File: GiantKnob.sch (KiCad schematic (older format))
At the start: 65 parts

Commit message: First version of schematics
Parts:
- removed C? (x2): 1p, symbol device:C_Small
- removed R? (x2): 10k, symbol device:R_Small
- removed SW?: ENC1, symbol device:Rotary_Encoder_Switch
- removed SW?: ENC2, symbol device:Rotary_Encoder_Switch
- added SW4: ENC1, symbol device:Rotary_Encoder
- added SW7: ENC2, symbol device:Rotary_Encoder
- gave numbers to parts that had none: 53
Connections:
- net BTN1: now also U2.20 (PD2)
- net BTN2: now also U2.21 (PD3)
- net BTN3: now also U2.25 (PD4)
- net ENC1_A: now also U2.26 (PD6)
- net ENC1_B: now also U2.27 (PD7)
- net ENC2_A: now also U2.31 (PC6)
- net ENC2_B: now also U2.32 (PC7)
- net GND: now also SW4.C, SW7.C
- net VFO_A: now also U2.18 (PD0)
- net VFO_B: now also U2.19 (PD1)
- net VFO_BTN: now also U2.1 (PE6)
- net at C10.1, R8.2, U1.5: now also SW4.A
- net at C11.1, R9.2, U1.9: now also SW4.B
- net at C15.1, R14.2, U1.11: now also SW7.A
- net at C16.1, R15.2, U1.13: now also SW7.B
- no-connect marks 0 -> 10
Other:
- moved on the sheet: D4, R13, R17

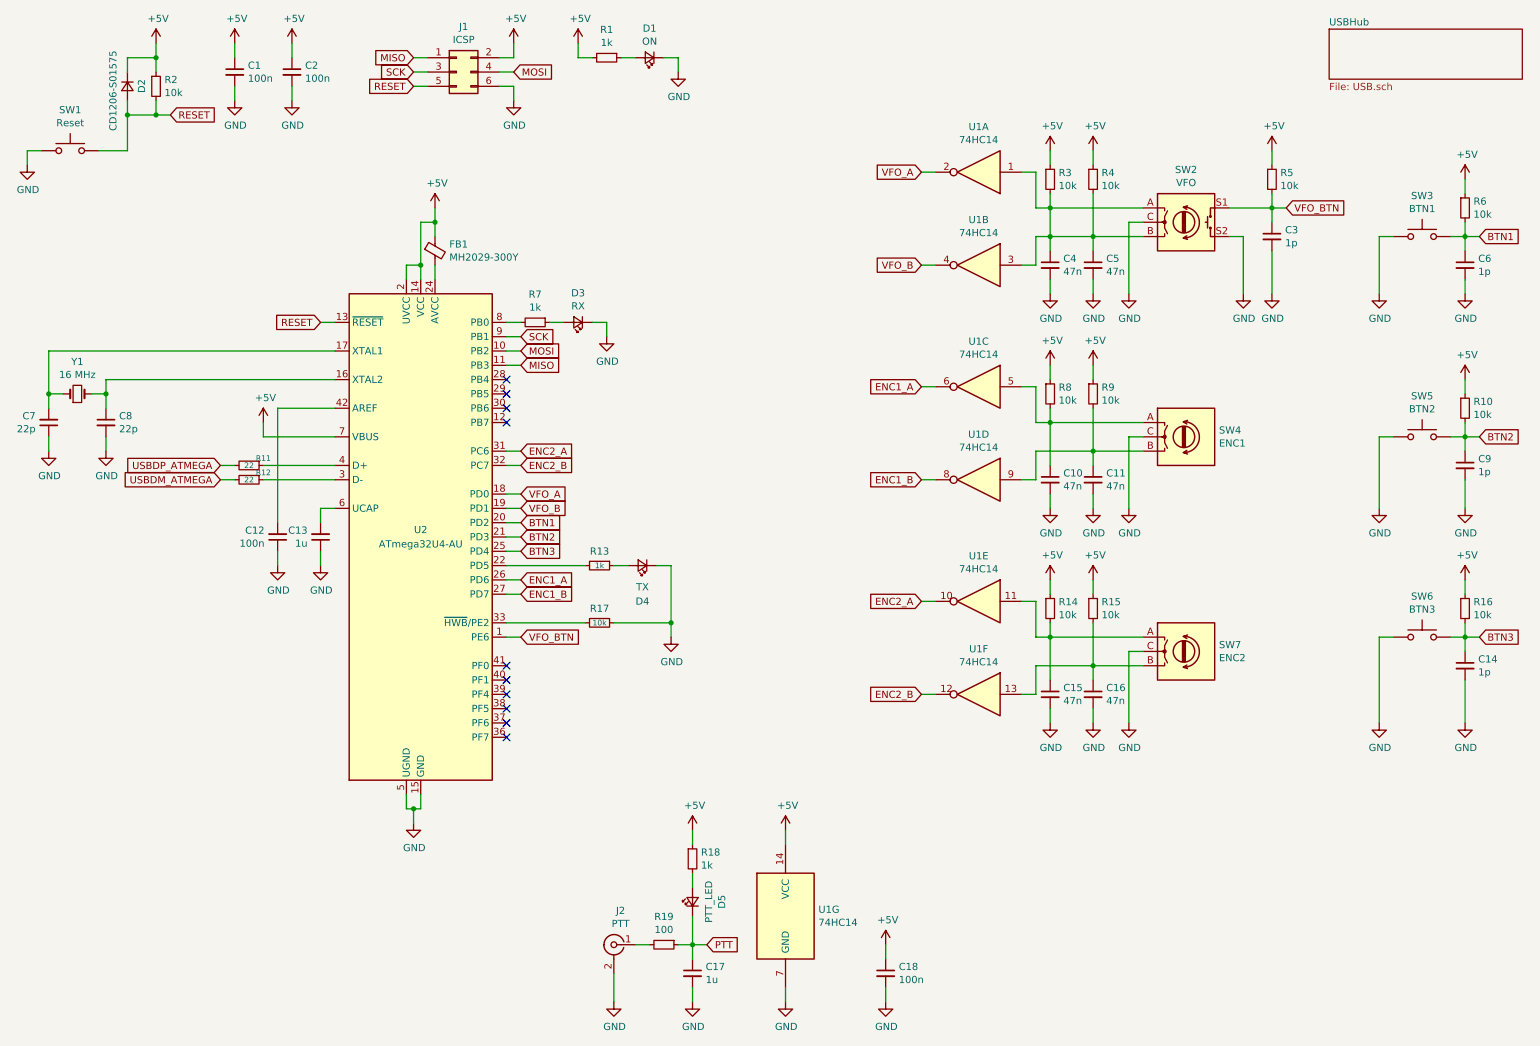
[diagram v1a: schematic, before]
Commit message: Added PTT to ATmega32U4
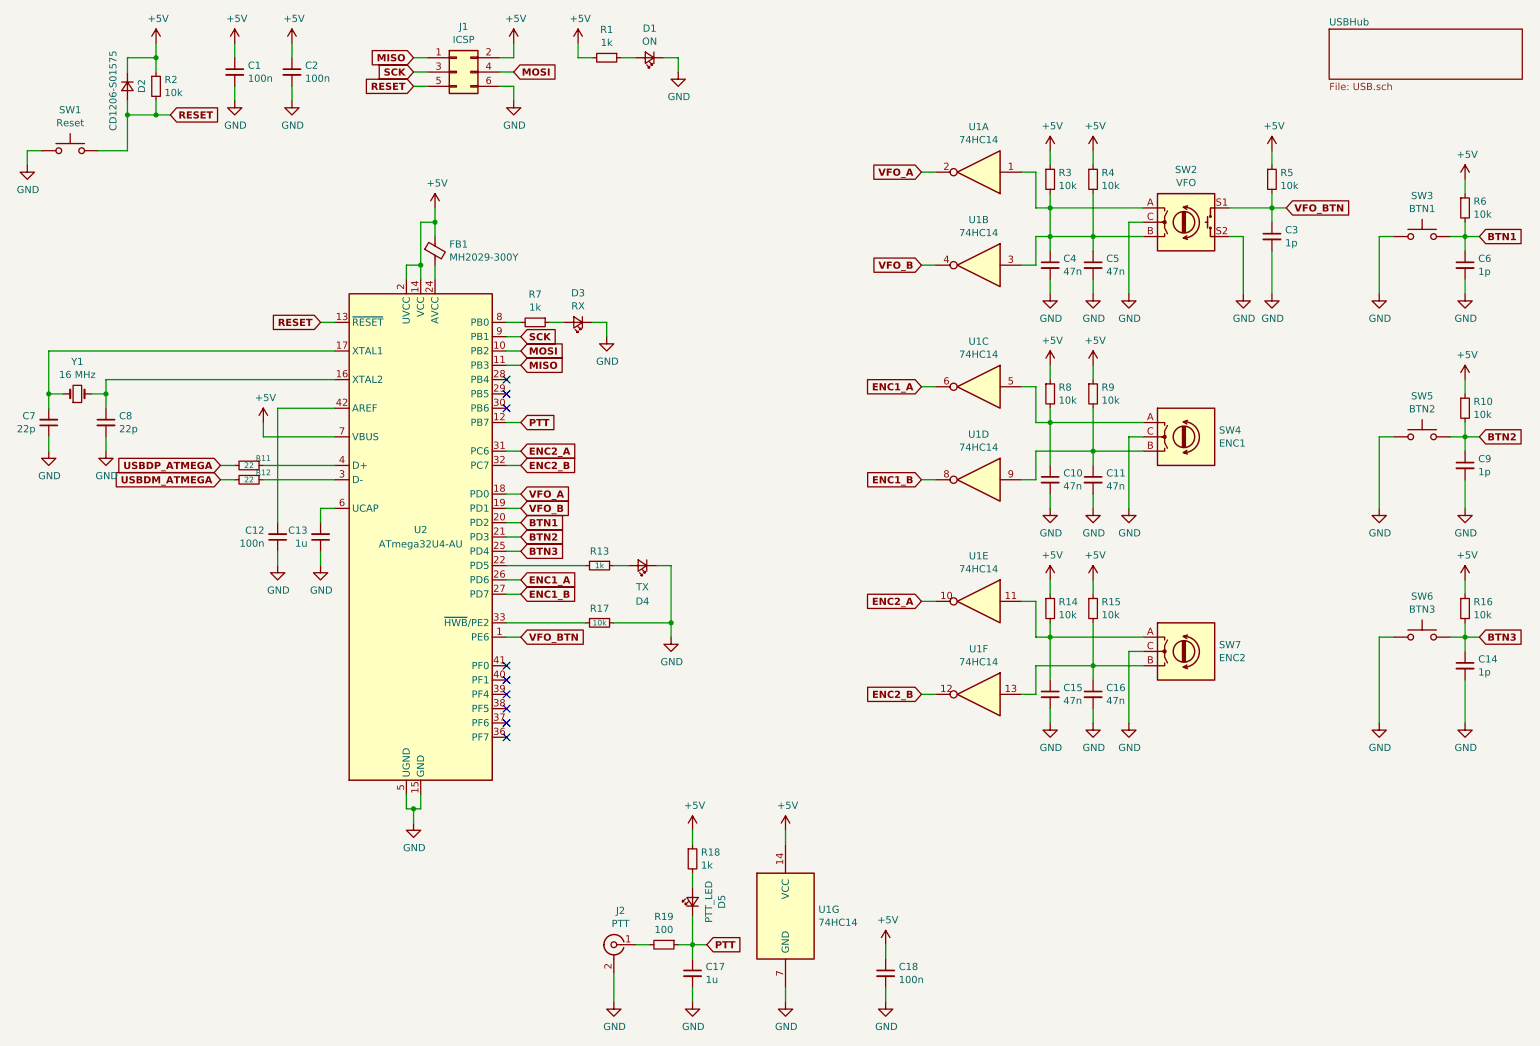
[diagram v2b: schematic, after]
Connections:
- net PTT: now also U2.12 (PB7)
- no-connect marks 10 -> 9
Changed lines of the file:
@@
 Wire Wire Line
 	2100 3800 2000 3800
-Text GLabel 2000 3700 0    50   Input ~ 0
+Text GLabel 2000 3700 0    50   Input ~ 6
 USBDP_ATMEGA
-Text GLabel 2000 3800 0    50   Input ~ 0
+Text GLabel 2000 3800 0    50   Input ~ 6
 USBDM_ATMEGA
 $Comp
@@
 	1    0    0    -1
 $EndComp
-Text GLabel 1650 1250 2    50   Input ~ 0
+Text GLabel 1650 1250 2    50   Input ~ 6
 RESET
 Wire Wire Line
 	1550 1250 1650 1250
 Connection ~ 1550 1250
-Text GLabel 2700 2700 0    50   Input ~ 0
+Text GLabel 2700 2700 0    50   Input ~ 6
 RESET
 Wire Wire Line
@@
 Wire Wire Line
 	4050 850  4050 750
-Text GLabel 4050 950  2    50   Input ~ 0
+Text GLabel 4050 950  2    50   Input ~ 6
 MOSI
-Text GLabel 3350 1050 0    50   Input ~ 0
+Text GLabel 3350 1050 0    50   Input ~ 6
 RESET
-Text GLabel 3350 950  0    50   Input ~ 0
+Text GLabel 3350 950  0    50   Input ~ 6
 SCK
-Text GLabel 3350 850  0    50   Input ~ 0
+Text GLabel 3350 850  0    50   Input ~ 6
 MISO
 Wire Wire Line
@@
 	1    0    0    -1
 $EndComp
-Text GLabel 4100 3000 2    50   Input ~ 0
+Text GLabel 4100 3000 2    50   Input ~ 6
 MISO
 Wire Wire Line
 	4000 3000 4100 3000
-Text GLabel 4100 2900 2    50   Input ~ 0
+Text GLabel 4100 2900 2    50   Input ~ 6
 MOSI
 Wire Wire Line
 	4000 2900 4100 2900
-Text GLabel 4100 2800 2    50   Input ~ 0
+Text GLabel 4100 2800 2    50   Input ~ 6
 SCK
 Wire Wire Line
@@
 Wire Wire Line
 	10700 2100 10800 2100
-Text GLabel 10800 2100 2    50   Input ~ 0
+Text GLabel 10800 2100 2    50   Input ~ 6
 BTN1
 $Comp
@@
 Wire Wire Line
 	10700 3500 10800 3500
-Text GLabel 10800 3500 2    50   Input ~ 0
+Text GLabel 10800 3500 2    50   Input ~ 6
 BTN2
 $Comp
@@
 Wire Wire Line
 	10700 4900 10800 4900
-Text GLabel 10800 4900 2    50   Input ~ 0
+Text GLabel 10800 4900 2    50   Input ~ 6
 BTN3
 Wire Wire Line
@@
 	1    0    0    -1
 $EndComp
-Text GLabel 9450 1900 2    50   Input ~ 0
+Text GLabel 9450 1900 2    50   Input ~ 6
 VFO_BTN
 Wire Wire Line
@@
 Wire Wire Line
 	7000 1650 6900 1650
-Text GLabel 6900 1650 0    50   Input ~ 0
+Text GLabel 6900 1650 0    50   Input ~ 6
 VFO_A
 Wire Wire Line
@@
 Wire Wire Line
 	7000 2300 6900 2300
-Text GLabel 6900 2300 0    50   Input ~ 0
+Text GLabel 6900 2300 0    50   Input ~ 6
 VFO_B
 $Comp
@@
 Wire Wire Line
 	7000 3150 6900 3150
-Text GLabel 6900 3150 0    50   Input ~ 0
+Text GLabel 6900 3150 0    50   Input ~ 6
 ENC1_A
 Wire Wire Line
@@
 Wire Wire Line
 	7000 3800 6900 3800
-Text GLabel 6900 3800 0    50   Input ~ 0
+Text GLabel 6900 3800 0    50   Input ~ 6
 ENC1_B
 $Comp
@@
 Wire Wire Line
 	7000 4650 6900 4650
-Text GLabel 6900 4650 0    50   Input ~ 0
+Text GLabel 6900 4650 0    50   Input ~ 6
 ENC2_A
 Wire Wire Line
@@
 Wire Wire Line
 	7000 5300 6900 5300
-Text GLabel 6900 5300 0    50   Input ~ 0
+Text GLabel 6900 5300 0    50   Input ~ 6
 ENC2_B
 $Comp
@@
 Wire Wire Line
 	5300 7050 5400 7050
-Text GLabel 5400 7050 2    50   Input ~ 0
+Text GLabel 5400 7050 2    50   Input ~ 6
 PTT
 $Comp
@@
 NoConn ~ 4000 5500
 NoConn ~ 4000 5600
-Text GLabel 4100 3900 2    50   Input ~ 0
+Text GLabel 4100 3900 2    50   Input ~ 6
 VFO_A
-Text GLabel 4100 4000 2    50   Input ~ 0
+Text GLabel 4100 4000 2    50   Input ~ 6
 VFO_B
 Wire Wire Line
@@
 Wire Wire Line
 	4000 4000 4100 4000
-Text GLabel 4100 4100 2    50   Input ~ 0
+Text GLabel 4100 4100 2    50   Input ~ 6
 BTN1
 Wire Wire Line
 	4000 4100 4100 4100
-Text GLabel 4100 4200 2    50   Input ~ 0
+Text GLabel 4100 4200 2    50   Input ~ 6
 BTN2
 Wire Wire Line
 	4000 4200 4100 4200
-Text GLabel 4100 4300 2    50   Input ~ 0
+Text GLabel 4100 4300 2    50   Input ~ 6
 BTN3
 Wire Wire Line
 	4000 4300 4100 4300
-Text GLabel 4100 4900 2    50   Input ~ 0
+Text GLabel 4100 4900 2    50   Input ~ 6
 VFO_BTN
 Wire Wire Line
 	4000 4900 4100 4900
-Text GLabel 4100 4500 2    50   Input ~ 0
+Text GLabel 4100 4500 2    50   Input ~ 6
 ENC1_A
-Text GLabel 4100 4600 2    50   Input ~ 0
+Text GLabel 4100 4600 2    50   Input ~ 6
 ENC1_B
 Wire Wire Line
@@
 	1    0    0    -1
 $EndComp
-Text GLabel 4100 3600 2    50   Input ~ 0
+Text GLabel 4100 3600 2    50   Input ~ 6
 ENC2_A
-Text GLabel 4100 3700 2    50   Input ~ 0
+Text GLabel 4100 3700 2    50   Input ~ 6
 ENC2_B
 Wire Wire Line
@@
 NoConn ~ 4000 3200
 NoConn ~ 4000 3300
-NoConn ~ 4000 3400
 Wire Wire Line
 	5150 4400 5150 4800
@@
 Wire Wire Line
 	5150 4800 5150 4900
+Text GLabel 4100 3400 2    50   Input ~ 6
+PTT
+Wire Wire Line
+	4000 3400 4100 3400
 $EndSCHEMATC

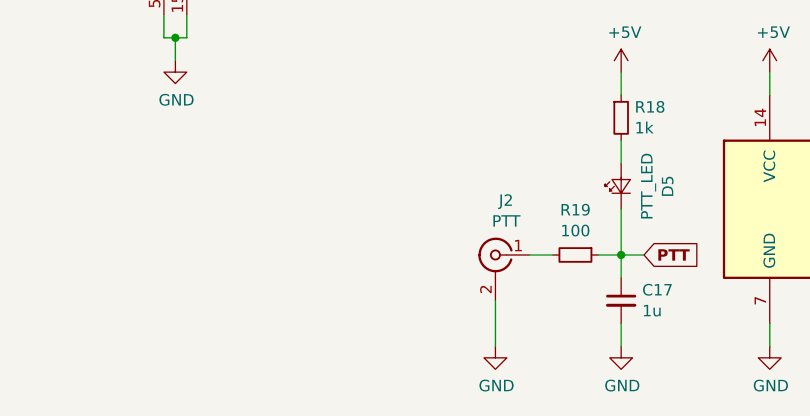
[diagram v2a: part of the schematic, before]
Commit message: Added component footprints
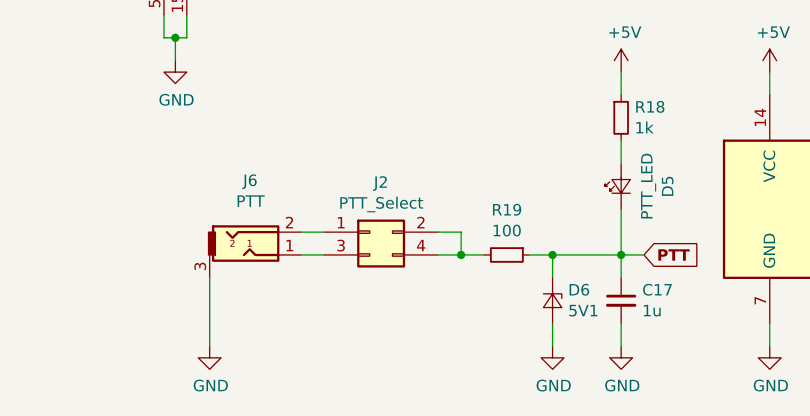
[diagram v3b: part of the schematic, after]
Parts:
- removed J2: PTT, symbol conn:Conn_Coaxial
- added D6: 5V1, Diodes_SMD:D_SOD-123, symbol device:D_Zener_Small
- added J2: PTT_Select, Pin_Headers:Pin_Header_Straight_2x02_Pitch2.54mm_SMD, symbol conn:Conn_02x02_Odd_Even
- added J6: PTT, GiantKnob:PJ-320B, symbol conn:Audio-Jack-3
- C1, C10, C11, C12, C13, C14, C15, C16, C17, C18, C2, C3, C4, C5, C6, C7, C8, C9: footprint (none) -> Capacitors_SMD:C_0603
- D1, D3, D4, D5: footprint (none) -> LEDs:LED_0805
- D2: footprint (none) -> Diodes_SMD:D_1206
- FB1: footprint (none) -> Inductors_SMD:L_0805
- J1: footprint (none) -> Pin_Headers:Pin_Header_Straight_2x03_Pitch2.54mm_SMD
- R1, R10, R11, R12, R13, R14, R15, R16, R17, R18, R19, R2, R3, R4, R5, R6, R7, R8, R9: footprint (none) -> Resistors_SMD:R_0603
- SW1: footprint (none) -> Buttons_Switches_SMD:SW_SPST_PTS645
- SW2: footprint (none) -> Rotary_Encoder:RotaryEncoder_Alps_EC12E-Switch_Vertical_H20mm
- SW3, SW5, SW6: footprint (none) -> Buttons_Switches_THT:SW_PUSH-12mm
- SW4, SW7: footprint (none) -> Rotary_Encoder:RotaryEncoder_Alps_EC12E_Vertical_H20mm
- U1: footprint (none) -> Housings_SOIC:SOIC-14_3.9x8.7mm_Pitch1.27mm
- U2: footprint Package_QFP:TQFP-44_10x10mm_P0.8mm -> Housings_QFP:TQFP-44_10x10mm_Pitch0.8mm
- Y1: footprint (none) -> Crystals:Crystal_SMD_5032-2pin_5.0x3.2mm
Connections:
- net GND: now also D6.2 (A), J6.3
- net PTT: now also D6.1 (K)
- net at R19.2: now also J2.2 (Pin_2), J2.4 (Pin_4)
- new net: J2.3 (Pin_3), J6.1
- new net: J2.1 (Pin_1), J6.2
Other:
- moved on the sheet: R19

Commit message: Board layout for prototype
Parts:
- removed D3: RX, LEDs:LED_0805, symbol GiantKnob-rescue:LED_Small-Device
- removed D4: TX, LEDs:LED_0805, symbol GiantKnob-rescue:LED_Small-Device
- removed R13, R7: 1k, Resistors_SMD:R_0603, symbol GiantKnob-rescue:R_Small-Device
- C1, C12, C13, C18, C2, C7, C8: footprint Capacitors_SMD:C_0603 -> Capacitor_SMD:C_0603_1608Metric
- C10, C11, C14, C15, C16, C17, C3, C4, C5, C6, C9: footprint Capacitors_SMD:C_0603 -> Capacitor_SMD:C_0603_1608Metric; symbol device:C_Small -> GiantKnob-rescue:C_Small-device
- D1, D5: footprint LEDs:LED_0805 -> LED_SMD:LED_0805_2012Metric
- D2: footprint Diodes_SMD:D_1206 -> Diode_SMD:D_1206_3216Metric
- D6: footprint Diodes_SMD:D_SOD-123 -> Diode_SMD:D_SOD-123; symbol device:D_Zener_Small -> GiantKnob-rescue:D_Zener_Small-device
- FB1: footprint Inductors_SMD:L_0805 -> Inductor_SMD:L_0805_2012Metric
- J1: footprint Pin_Headers:Pin_Header_Straight_2x03_Pitch2.54mm_SMD -> Connector_PinHeader_2.54mm:PinHeader_2x03_P2.54mm_Vertical_SMD
- J2: footprint Pin_Headers:Pin_Header_Straight_2x02_Pitch2.54mm_SMD -> Connector_PinHeader_2.54mm:PinHeader_2x02_P2.54mm_Vertical_SMD; symbol conn:Conn_02x02_Odd_Even -> GiantKnob-rescue:Conn_02x02_Odd_Even-conn
- J6: symbol conn:Audio-Jack-3 -> GiantKnob-rescue:Audio-Jack-3-conn
- R1, R11, R12, R17, R2: footprint Resistors_SMD:R_0603 -> Resistor_SMD:R_0603_1608Metric
- R10, R14, R15, R16, R18, R19, R3, R4, R5, R6, R8, R9: footprint Resistors_SMD:R_0603 -> Resistor_SMD:R_0603_1608Metric; symbol device:R_Small -> GiantKnob-rescue:R_Small-device
- SW1: footprint Buttons_Switches_SMD:SW_SPST_PTS645 -> Button_Switch_SMD:SW_SPST_PTS645
- SW2: symbol device:Rotary_Encoder_Switch -> GiantKnob-rescue:Rotary_Encoder_Switch-device
- SW3, SW5, SW6: footprint Buttons_Switches_THT:SW_PUSH-12mm -> Button_Switch_THT:SW_PUSH-12mm
- SW4, SW7: symbol device:Rotary_Encoder -> GiantKnob-rescue:Rotary_Encoder-device
- U1: footprint Housings_SOIC:SOIC-14_3.9x8.7mm_Pitch1.27mm -> Package_SO:SOIC-14_3.9x8.7mm_P1.27mm
- U2: footprint Housings_QFP:TQFP-44_10x10mm_Pitch0.8mm -> Package_QFP:TQFP-44_10x10mm_P0.8mm
- Y1: footprint Crystals:Crystal_SMD_5032-2pin_5.0x3.2mm -> Crystal:Crystal_SMD_5032-2Pin_5.0x3.2mm
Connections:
- net VFO_BTN: now also U2.22 (PD5); no longer U2.1 (PE6)
- net at C4.1, R3.2, SW2.A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: no longer C5.1, R4.2, SW2.B, U1.3
- new net: C5.1, R4.2, SW2.B, U1.3

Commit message: Prototype v1
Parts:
- C14, C3, C6, C9: value 1p -> 1u
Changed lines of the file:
@@
 P 10700 2300
 F 0 "C6" H 10792 2346 50  0000 L CNN
-F 1 "1p" H 10792 2255 50  0000 L CNN
+F 1 "1u" H 10792 2255 50  0000 L CNN
 F 2 "Capacitor_SMD:C_0603_1608Metric" H 10700 2300 50  0001 C CNN
 F 3 "~" H 10700 2300 50  0001 C CNN
@@
 P 10700 3700
 F 0 "C9" H 10792 3746 50  0000 L CNN
-F 1 "1p" H 10792 3655 50  0000 L CNN
+F 1 "1u" H 10792 3655 50  0000 L CNN
 F 2 "Capacitor_SMD:C_0603_1608Metric" H 10700 3700 50  0001 C CNN
 F 3 "~" H 10700 3700 50  0001 C CNN
@@
 P 10700 5100
 F 0 "C14" H 10792 5146 50  0000 L CNN
-F 1 "1p" H 10792 5055 50  0000 L CNN
+F 1 "1u" H 10792 5055 50  0000 L CNN
 F 2 "Capacitor_SMD:C_0603_1608Metric" H 10700 5100 50  0001 C CNN
 F 3 "~" H 10700 5100 50  0001 C CNN
@@
 P 9350 2100
 F 0 "C3" H 9442 2146 50  0000 L CNN
-F 1 "1p" H 9442 2055 50  0000 L CNN
+F 1 "1u" H 9442 2055 50  0000 L CNN
 F 2 "Capacitor_SMD:C_0603_1608Metric" H 9350 2100 50  0001 C CNN
 F 3 "~" H 9350 2100 50  0001 C CNN
